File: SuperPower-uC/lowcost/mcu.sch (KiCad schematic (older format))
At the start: 5 parts, among them J5 main pin header, J6 main pin header, U13 ESP32-WROOM32

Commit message: schematic layout cleaning
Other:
- note added: "MCU"
- note added: "Main pin Headers\n"
- note added: "labels\n"
- moved on the sheet: C19, C20, J5, J6, U13

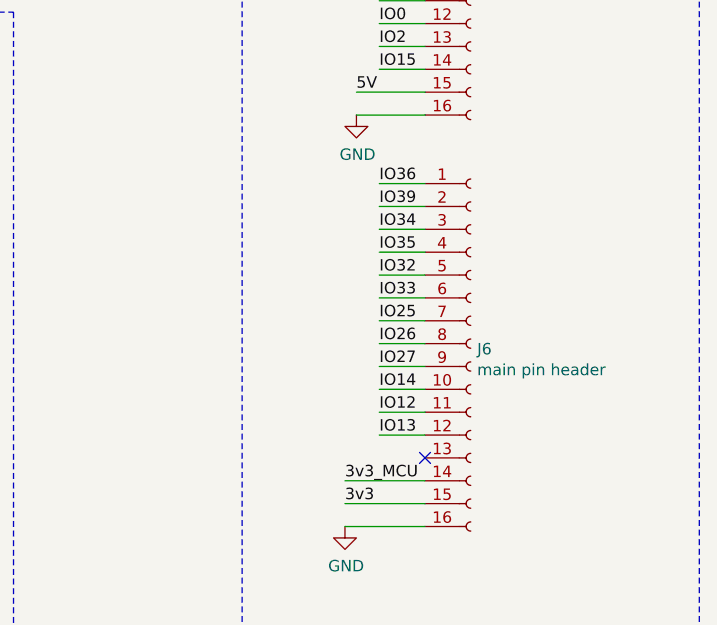
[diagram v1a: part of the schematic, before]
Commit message: added rst to main header
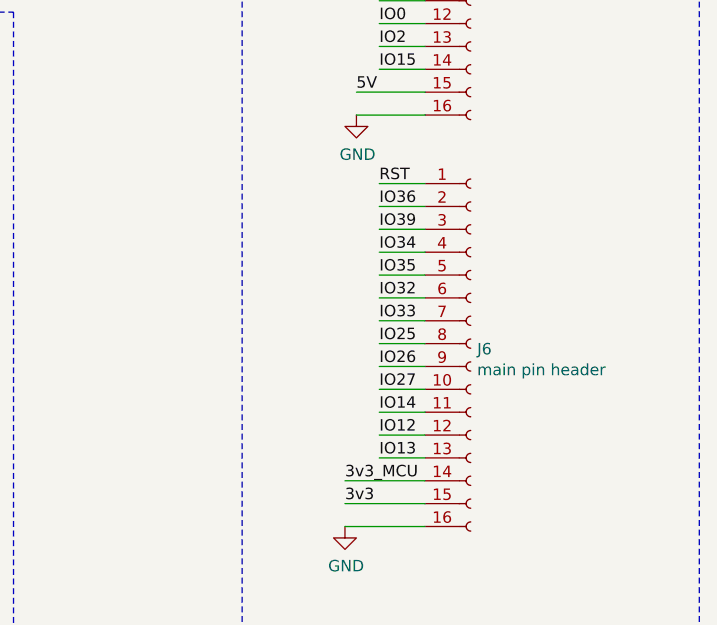
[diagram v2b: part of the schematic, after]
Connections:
- net IO12: now also J6.12 (Pin_12); no longer J6.11 (Pin_11)
- net IO13: now also J6.13 (Pin_13); no longer J6.12 (Pin_12)
- net IO14: now also J6.11 (Pin_11); no longer J6.10 (Pin_10)
- net IO25: now also J6.8 (Pin_8); no longer J6.7 (Pin_7)
- net IO26: now also J6.9 (Pin_9); no longer J6.8 (Pin_8)
- net IO27: now also J6.10 (Pin_10); no longer J6.9 (Pin_9)
- net IO32: now also J6.6 (Pin_6); no longer J6.5 (Pin_5)
- net IO33: now also J6.7 (Pin_7); no longer J6.6 (Pin_6)
- net IO34: now also J6.4 (Pin_4); no longer J6.3 (Pin_3)
- net IO35: now also J6.5 (Pin_5); no longer J6.4 (Pin_4)
- net IO36: now also J6.2 (Pin_2); no longer J6.1 (Pin_1)
- net IO39: now also J6.3 (Pin_3); no longer J6.2 (Pin_2)
- net RST: now also J6.1 (Pin_1)
- no-connect marks 8 -> 7
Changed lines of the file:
@@
 IO23
 Wire Wire Line
-	9800 3050 9600 3050
-Wire Wire Line
 	9800 3150 9600 3150
 Wire Wire Line
@@
 	9800 3550 9600 3550
 Wire Wire Line
-	9800 3750 9600 3750
-Wire Wire Line
-	9600 3650 9800 3650
+	9800 3650 9600 3650
 Wire Wire Line
 	9800 3850 9600 3850
 Wire Wire Line
-	9600 3950 9800 3950
+	9600 3750 9800 3750
+Wire Wire Line
+	9800 3950 9600 3950
 Wire Wire Line
 	9600 4050 9800 4050
-Text Label 9600 3050 0    50   ~ 0
+Wire Wire Line
+	9600 4150 9800 4150
+Text Label 9600 3150 0    50   ~ 0
 IO36
-Text Label 9600 3150 0    50   ~ 0
+Text Label 9600 3250 0    50   ~ 0
 IO39
-Text Label 9600 3250 0    50   ~ 0
+Text Label 9600 3350 0    50   ~ 0
 IO34
-Text Label 9600 3350 0    50   ~ 0
+Text Label 9600 3450 0    50   ~ 0
 IO35
-Text Label 9600 3450 0    50   ~ 0
+Text Label 9600 3550 0    50   ~ 0
 IO32
-Text Label 9600 3550 0    50   ~ 0
+Text Label 9600 3650 0    50   ~ 0
 IO33
-Text Label 9600 3650 0    50   ~ 0
+Text Label 9600 3750 0    50   ~ 0
 IO25
-Text Label 9600 3750 0    50   ~ 0
+Text Label 9600 3850 0    50   ~ 0
 IO26
-Text Label 9600 3850 0    50   ~ 0
+Text Label 9600 3950 0    50   ~ 0
 IO27
-Text Label 9600 3950 0    50   ~ 0
+Text Label 9600 4050 0    50   ~ 0
 IO14
-Text Label 9600 4050 0    50   ~ 0
+Text Label 9600 4150 0    50   ~ 0
 IO12
 Wire Wire Line
-	9800 4150 9600 4150
-Text Label 9600 4150 0    50   ~ 0
+	9800 4250 9600 4250
+Text Label 9600 4250 0    50   ~ 0
 IO13
 Wire Wire Line
@@
 	1    0    0    -1
 $EndComp
-NoConn ~ 9800 4250
 Wire Wire Line
 	4150 2950 4350 2950
@@
 Text Notes 9100 850  0    50   ~ 0
 Main pin Headers\n
+Text Label 9600 3050 0    50   ~ 0
+RST
+Wire Wire Line
+	9600 3050 9800 3050
 $EndSCHEMATC

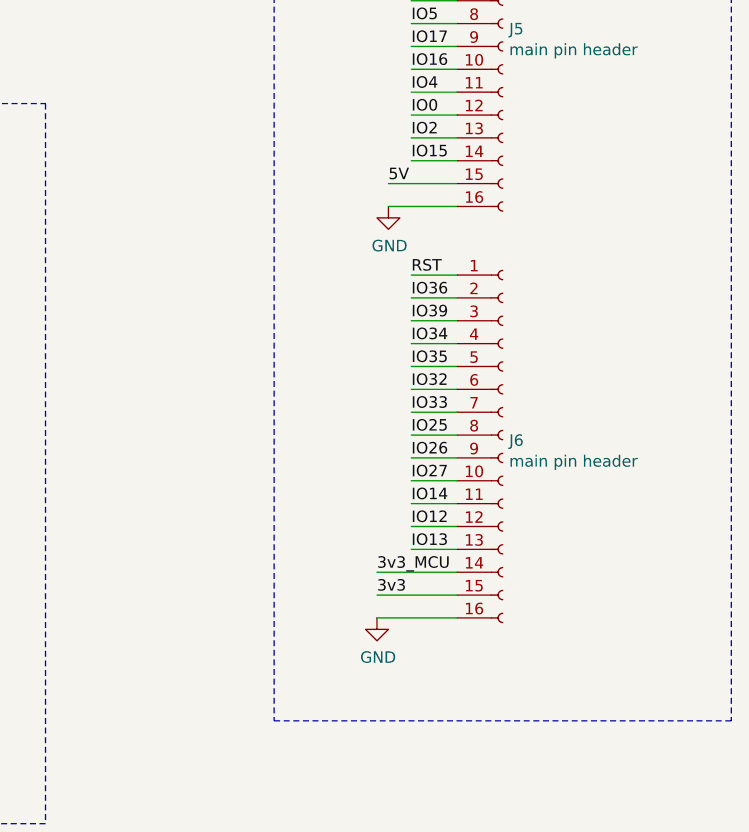
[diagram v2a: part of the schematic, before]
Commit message: added 100R to protection ic and some minor other stuff
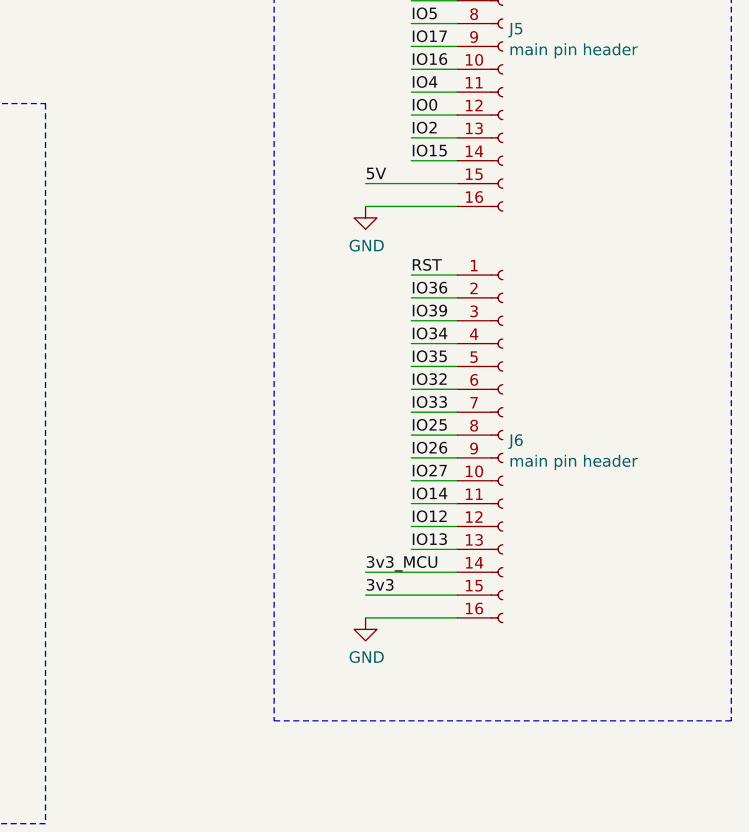
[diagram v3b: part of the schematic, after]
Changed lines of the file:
@@
 IO13
 Wire Wire Line
-	9800 4550 9450 4550
+	9800 4550 9400 4550
 Wire Wire Line
-	9800 2750 9500 2750
+	9800 2750 9400 2750
 $Comp
 L power:GND #PWR0119
 U 1 1 5F8C9874
-P 9500 2750
-F 0 "#PWR0119" H 9500 2500 50  0001 C CNN
-F 1 "GND" H 9505 2577 50  0000 C CNN
-F 2 "" H 9500 2750 50  0001 C CNN
-F 3 "" H 9500 2750 50  0001 C CNN
-	1    9500 2750
+P 9400 2750
+F 0 "#PWR0119" H 9400 2500 50  0001 C CNN
+F 1 "GND" H 9405 2577 50  0000 C CNN
+F 2 "" H 9400 2750 50  0001 C CNN
+F 3 "" H 9400 2750 50  0001 C CNN
+	1    9400 2750
 	1    0    0    -1
 $EndComp
@@
 L power:GND #PWR0120
 U 1 1 5F8C9F4B
-P 9450 4550
-F 0 "#PWR0120" H 9450 4300 50  0001 C CNN
-F 1 "GND" H 9455 4377 50  0000 C CNN
-F 2 "" H 9450 4550 50  0001 C CNN
-F 3 "" H 9450 4550 50  0001 C CNN
-	1    9450 4550
+P 9400 4550
+F 0 "#PWR0120" H 9400 4300 50  0001 C CNN
+F 1 "GND" H 9405 4377 50  0000 C CNN
+F 2 "" H 9400 4550 50  0001 C CNN
+F 3 "" H 9400 4550 50  0001 C CNN
+	1    9400 4550
 	1    0    0    -1
 $EndComp
@@
 Text Notes 3500 2450 0    50   ~ 0
 MCU
-Text Label 9500 2650 0    50   ~ 0
+Text Label 9400 2650 0    50   ~ 0
 5V
-Text Label 9450 4450 0    50   ~ 0
+Text Label 9400 4450 0    50   ~ 0
 3v3
 Wire Wire Line
-	9450 4450 9800 4450
+	9400 4450 9800 4450
 Wire Wire Line
-	9800 4350 9450 4350
-Text Label 9450 4350 0    50   ~ 0
+	9800 4350 9400 4350
+Text Label 9400 4350 0    50   ~ 0
 3v3_MCU
 Text Label 3950 3250 0    50   ~ 0
@@
 5V
 Wire Wire Line
-	9500 2650 9800 2650
+	9400 2650 9800 2650
 Wire Notes Line
 	600  650  1850 650

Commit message: modified pin headers to fit devkit version
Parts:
- removed J5, J6: main pin header, Connector_PinHeader_2.54mm:PinHeader_1x16_P2.54mm_Vertical, symbol Connector:Conn_01x16_Female
- added J5: main pin header right, symbol Connector:Conn_01x17_Female
- added J6: main pin header left, symbol Connector:Conn_01x17_Female
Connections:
- net labels added: Vin
- wire segments 80 -> 83
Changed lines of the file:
@@
 $Descr A4 11693 8268
 encoding utf-8
-Sheet 6 7
+Sheet 5 7
 Title "SuperPower-uC"
 Date "2020-09-20"
@@
 Text HLabel 1150 1750 0    50   Input ~ 0
 GPIO0
-$Comp
-L Connector:Conn_01x16_Female J5
-U 1 1 5F88CF74
-P 10000 1950
-F 0 "J5" H 10028 1926 50  0000 L CNN
-F 1 "main pin header" H 10028 1835 50  0000 L CNN
-F 2 "Connector_PinHeader_2.54mm:PinHeader_1x16_P2.54mm_Vertical" H 10000 1950 50  0001 C CNN
-F 3 "~" H 10000 1950 50  0001 C CNN
-	1    10000 1950
-	1    0    0    -1
-$EndComp
-$Comp
-L Connector:Conn_01x16_Female J6
-U 1 1 5F896962
-P 10000 3750
-F 0 "J6" H 10028 3726 50  0000 L CNN
-F 1 "main pin header" H 10028 3635 50  0000 L CNN
-F 2 "Connector_PinHeader_2.54mm:PinHeader_1x16_P2.54mm_Vertical" H 10000 3750 50  0001 C CNN
-F 3 "~" H 10000 3750 50  0001 C CNN
-	1    10000 3750
-	1    0    0    -1
-$EndComp
 Wire Wire Line
 	5200 3250 4350 3250
@@
 IO23
 Wire Wire Line
-	9800 3150 9600 3150
-Wire Wire Line
 	9800 3250 9600 3250
 Wire Wire Line
@@
 	9800 3650 9600 3650
 Wire Wire Line
-	9800 3850 9600 3850
-Wire Wire Line
-	9600 3750 9800 3750
+	9800 3750 9600 3750
 Wire Wire Line
 	9800 3950 9600 3950
 Wire Wire Line
-	9600 4050 9800 4050
+	9600 3850 9800 3850
+Wire Wire Line
+	9800 4050 9600 4050
 Wire Wire Line
 	9600 4150 9800 4150
-Text Label 9600 3150 0    50   ~ 0
+Wire Wire Line
+	9600 4250 9800 4250
+Text Label 9600 3250 0    50   ~ 0
 IO36
-Text Label 9600 3250 0    50   ~ 0
+Text Label 9600 3350 0    50   ~ 0
 IO39
-Text Label 9600 3350 0    50   ~ 0
+Text Label 9600 3450 0    50   ~ 0
 IO34
-Text Label 9600 3450 0    50   ~ 0
+Text Label 9600 3550 0    50   ~ 0
 IO35
-Text Label 9600 3550 0    50   ~ 0
+Text Label 9600 3650 0    50   ~ 0
 IO32
-Text Label 9600 3650 0    50   ~ 0
+Text Label 9600 3750 0    50   ~ 0
 IO33
-Text Label 9600 3750 0    50   ~ 0
+Text Label 9600 3850 0    50   ~ 0
 IO25
-Text Label 9600 3850 0    50   ~ 0
+Text Label 9600 3950 0    50   ~ 0
 IO26
-Text Label 9600 3950 0    50   ~ 0
+Text Label 9600 4050 0    50   ~ 0
 IO27
-Text Label 9600 4050 0    50   ~ 0
+Text Label 9600 4150 0    50   ~ 0
 IO14
-Text Label 9600 4150 0    50   ~ 0
+Text Label 9600 4250 0    50   ~ 0
 IO12
 Wire Wire Line
-	9800 4250 9600 4250
-Text Label 9600 4250 0    50   ~ 0
+	9800 4350 9600 4350
+Text Label 9600 4350 0    50   ~ 0
 IO13
 Wire Wire Line
-	9800 4550 9400 4550
-Wire Wire Line
-	9800 2750 9400 2750
-$Comp
-L power:GND #PWR0119
-U 1 1 5F8C9874
-P 9400 2750
-F 0 "#PWR0119" H 9400 2500 50  0001 C CNN
-F 1 "GND" H 9405 2577 50  0000 C CNN
-F 2 "" H 9400 2750 50  0001 C CNN
-F 3 "" H 9400 2750 50  0001 C CNN
-	1    9400 2750
-	1    0    0    -1
-$EndComp
+	9800 4450 9250 4450
 $Comp
 L power:GND #PWR0120
 U 1 1 5F8C9F4B
-P 9400 4550
-F 0 "#PWR0120" H 9400 4300 50  0001 C CNN
-F 1 "GND" H 9405 4377 50  0000 C CNN
-F 2 "" H 9400 4550 50  0001 C CNN
-F 3 "" H 9400 4550 50  0001 C CNN
-	1    9400 4550
+P 9250 4450
+F 0 "#PWR0120" H 9250 4200 50  0001 C CNN
+F 1 "GND" H 9255 4277 50  0000 C CNN
+F 2 "" H 9250 4450 50  0001 C CNN
+F 3 "" H 9250 4450 50  0001 C CNN
+	1    9250 4450
 	1    0    0    -1
 $EndComp
@@
 	9600 2250 9800 2250
 Wire Wire Line
-	9600 2350 9800 2350
-Text Label 9600 2350 0    50   ~ 0
+	9600 1150 9800 1150
+Text Label 9600 1150 0    50   ~ 0
 IO0
 Text Label 9600 2250 0    50   ~ 0
@@
 IO23
 Wire Wire Line
-	9800 2450 9600 2450
-Text Label 9600 2450 0    50   ~ 0
+	9800 2350 9600 2350
+Text Label 9600 2350 0    50   ~ 0
 IO2
 Text Label 1250 1150 0    50   ~ 0
@@
 	1150 1750 1250 1750
 Wire Wire Line
-	9800 2550 9600 2550
-Text Label 9600 2550 0    50   ~ 0
+	9800 2450 9600 2450
+Text Label 9600 2450 0    50   ~ 0
 IO15
 Text HLabel 1100 2200 0    50   Input ~ 0
@@
 Text Notes 3500 2450 0    50   ~ 0
 MCU
+Text Label 9400 4650 0    50   ~ 0
+5V
+Wire Wire Line
+	9800 2650 9400 2650
 Text Label 9400 2650 0    50   ~ 0
-5V
-Text Label 9400 4450 0    50   ~ 0
-3v3
-Wire Wire Line
-	9400 4450 9800 4450
-Wire Wire Line
-	9800 4350 9400 4350
-Text Label 9400 4350 0    50   ~ 0
 3v3_MCU
 Text Label 3950 3250 0    50   ~ 0
@@
 5V
 Wire Wire Line
-	9400 2650 9800 2650
+	9400 4650 9800 4650
 Wire Notes Line
 	600  650  1850 650
@@
 Text Notes 9100 850  0    50   ~ 0
 Main pin Headers\n
-Text Label 9600 3050 0    50   ~ 0
+Text Label 9600 3150 0    50   ~ 0
 RST
 Wire Wire Line
-	9600 3050 9800 3050
+	9600 3150 9800 3150
+Wire Wire Line
+	9800 2550 9250 2550
+$Comp
+L power:GND #PWR?
+U 1 1 5F8D40E5
+P 9250 2550
+F 0 "#PWR?" H 9250 2300 50  0001 C CNN
+F 1 "GND" H 9255 2377 50  0000 C CNN
+F 2 "" H 9250 2550 50  0001 C CNN
+F 3 "" H 9250 2550 50  0001 C CNN
+	1    9250 2550
+	1    0    0    -1
+$EndComp
+$Comp
+L Connector:Conn_01x17_Female J5
+U 1 1 5F904645
+P 10000 1950
+F 0 "J5" H 10028 1976 50  0000 L CNN
+F 1 "main pin header right" H 10028 1885 50  0000 L CNN
+F 2 "" H 10000 1950 50  0001 C CNN
+F 3 "~" H 10000 1950 50  0001 C CNN
+	1    10000 1950
+	1    0    0    -1
+$EndComp
+$Comp
+L Connector:Conn_01x17_Female J6
+U 1 1 5F90988E
+P 10000 3850
+F 0 "J6" H 10028 3876 50  0000 L CNN
+F 1 "main pin header left" H 10028 3785 50  0000 L CNN
+F 2 "" H 10000 3850 50  0001 C CNN
+F 3 "~" H 10000 3850 50  0001 C CNN
+	1    10000 3850
+	1    0    0    -1
+$EndComp
+Text Label 9400 4550 0    50   ~ 0
+Vin
+Wire Wire Line
+	9400 4550 9800 4550
+Text HLabel 1100 2400 0    50   Output ~ 0
+Vin
+Wire Wire Line
+	1100 2400 1250 2400
+Text Label 1250 2400 0    50   ~ 0
+Vin
+Wire Wire Line
+	9400 2750 9800 2750
+Text Label 9400 2750 0    50   ~ 0
+3v3
+Wire Wire Line
+	9800 3050 9250 3050
+$Comp
+L power:GND #PWR?
+U 1 1 5F982B4C
+P 9250 3050
+F 0 "#PWR?" H 9250 2800 50  0001 C CNN
+F 1 "GND" H 9255 2877 50  0000 C CNN
+F 2 "" H 9250 3050 50  0001 C CNN
+F 3 "" H 9250 3050 50  0001 C CNN
+	1    9250 3050
+	1    0    0    -1
+$EndComp
 $EndSCHEMATC

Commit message: started pcb and added missing net labels
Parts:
- J5, J6: footprint (none) -> Connector_PinHeader_2.54mm:PinHeader_1x17_P2.54mm_Vertical
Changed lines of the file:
@@
 	9800 2550 9250 2550
 $Comp
-L power:GND #PWR?
+L power:GND #PWR0119
 U 1 1 5F8D40E5
 P 9250 2550
-F 0 "#PWR?" H 9250 2300 50  0001 C CNN
+F 0 "#PWR0119" H 9250 2300 50  0001 C CNN
 F 1 "GND" H 9255 2377 50  0000 C CNN
 F 2 "" H 9250 2550 50  0001 C CNN
@@
 F 0 "J5" H 10028 1976 50  0000 L CNN
 F 1 "main pin header right" H 10028 1885 50  0000 L CNN
-F 2 "" H 10000 1950 50  0001 C CNN
+F 2 "Connector_PinHeader_2.54mm:PinHeader_1x17_P2.54mm_Vertical" H 10000 1950 50  0001 C CNN
 F 3 "~" H 10000 1950 50  0001 C CNN
 	1    10000 1950
@@
 F 0 "J6" H 10028 3876 50  0000 L CNN
 F 1 "main pin header left" H 10028 3785 50  0000 L CNN
-F 2 "" H 10000 3850 50  0001 C CNN
+F 2 "Connector_PinHeader_2.54mm:PinHeader_1x17_P2.54mm_Vertical" H 10000 3850 50  0001 C CNN
 F 3 "~" H 10000 3850 50  0001 C CNN
 	1    10000 3850
@@
 	9800 3050 9250 3050
 $Comp
-L power:GND #PWR?
+L power:GND #PWR0128
 U 1 1 5F982B4C
 P 9250 3050
-F 0 "#PWR?" H 9250 2800 50  0001 C CNN
+F 0 "#PWR0128" H 9250 2800 50  0001 C CNN
 F 1 "GND" H 9255 2877 50  0000 C CNN
 F 2 "" H 9250 3050 50  0001 C CNN
